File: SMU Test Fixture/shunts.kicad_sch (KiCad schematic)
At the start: 17 parts

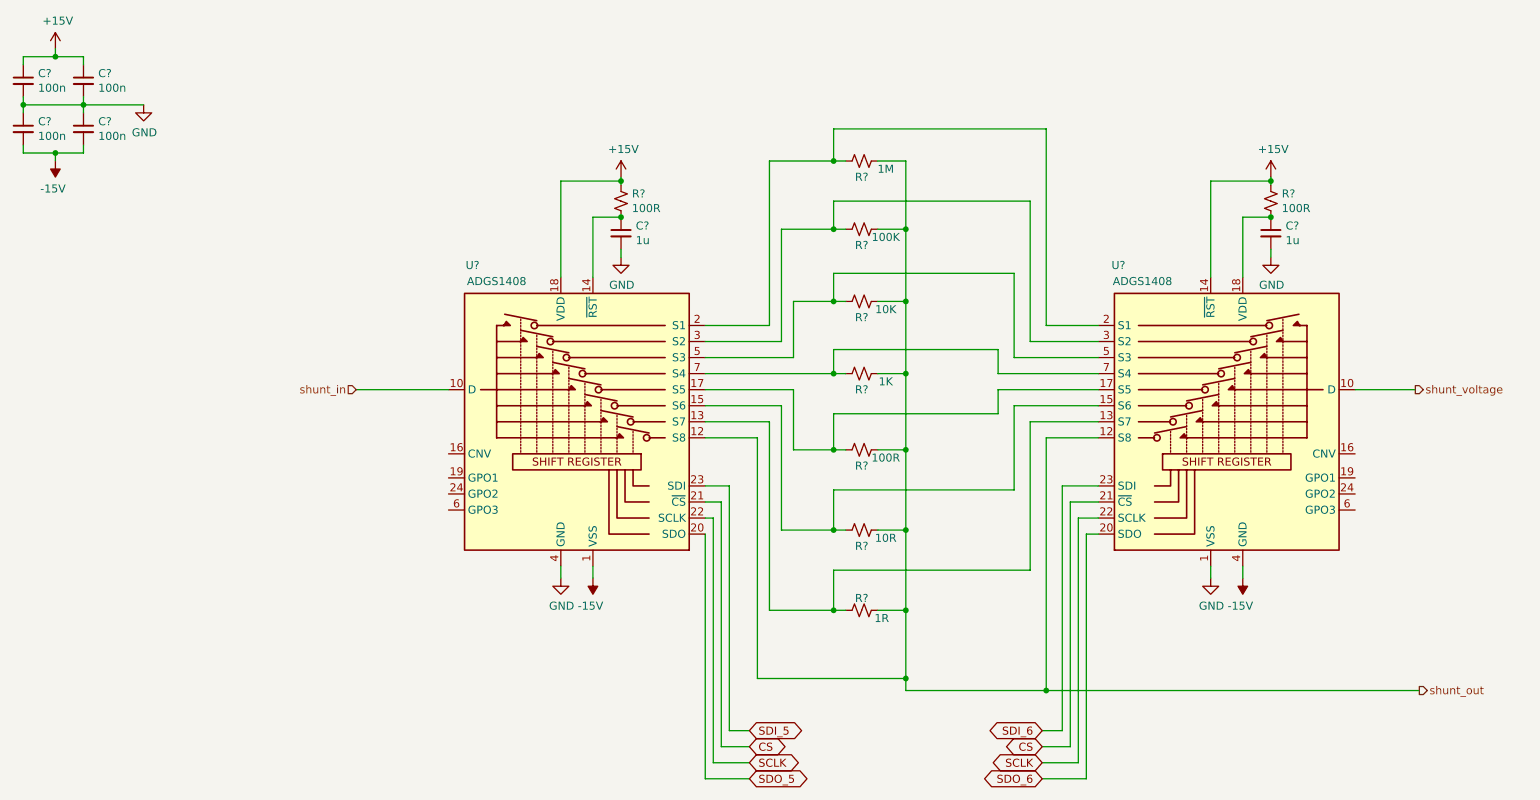
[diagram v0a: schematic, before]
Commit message: Fix grid nightmare. Begin adding bypass caps for a.switches
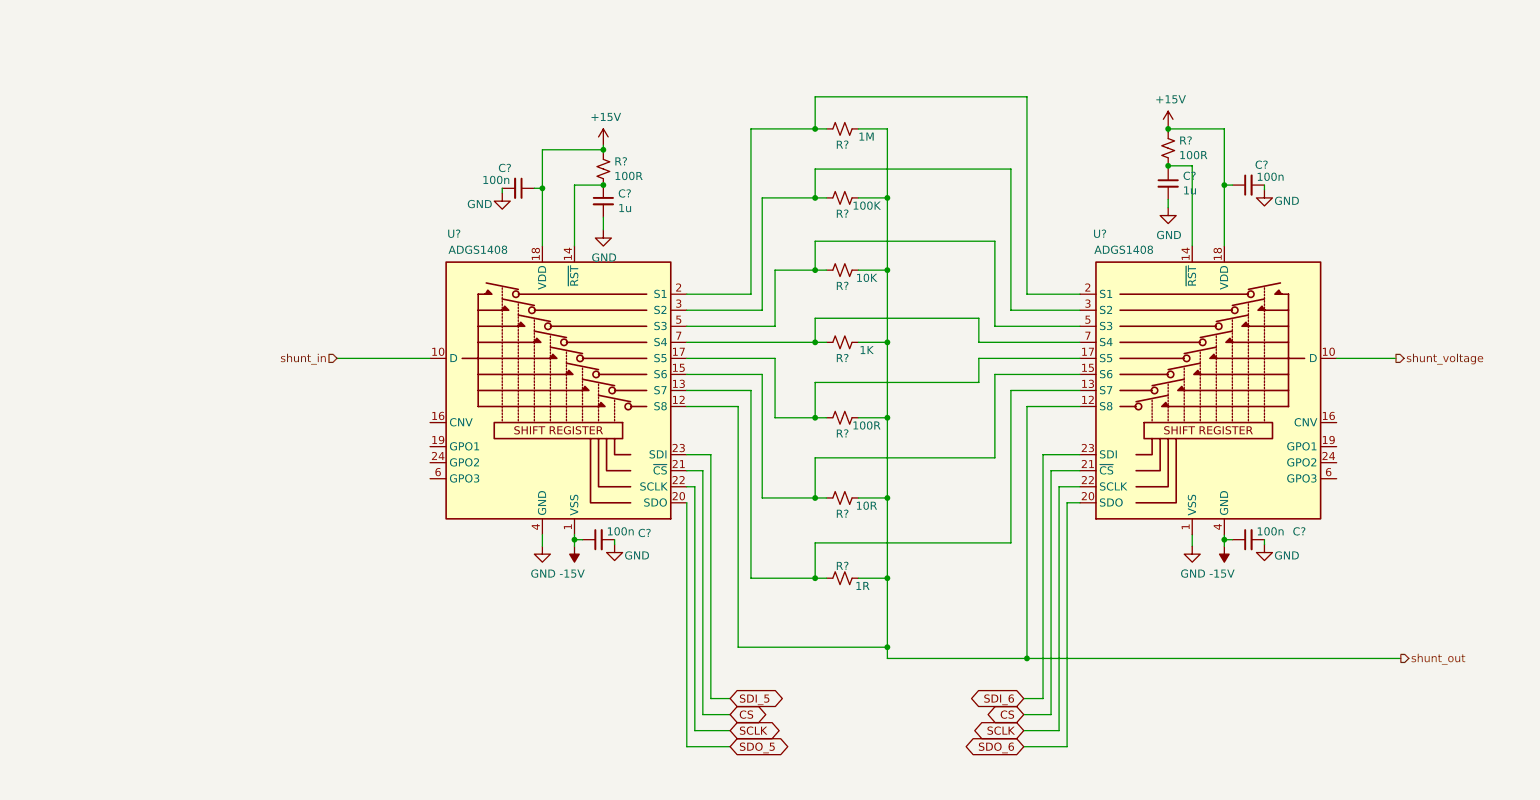
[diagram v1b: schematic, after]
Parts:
- removed C? (x4): 100n, Capacitor_SMD:C_0805_2012Metric_Pad1.18x1.45mm_HandSolder, symbol Device:C_Small
- added C? (x4): 100n, Capacitor_SMD:C_0805_2012Metric_Pad1.18x1.45mm_HandSolder, symbol Device:C_Small
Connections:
- net +15V: now also U?.18 (VDD), C?.1, C?.1; no longer U?.14 (~{RST})
- net -15V: now also C?.1, C?.1, C?.2, C?.2, C?.2, C?.2
- net at C?.1, R?.2: now also U?.14 (~{RST}); no longer U?.18 (VDD)
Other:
- moved on the sheet: C?, R?, U?

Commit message: Split ADGS1408 units, add switch contorl page
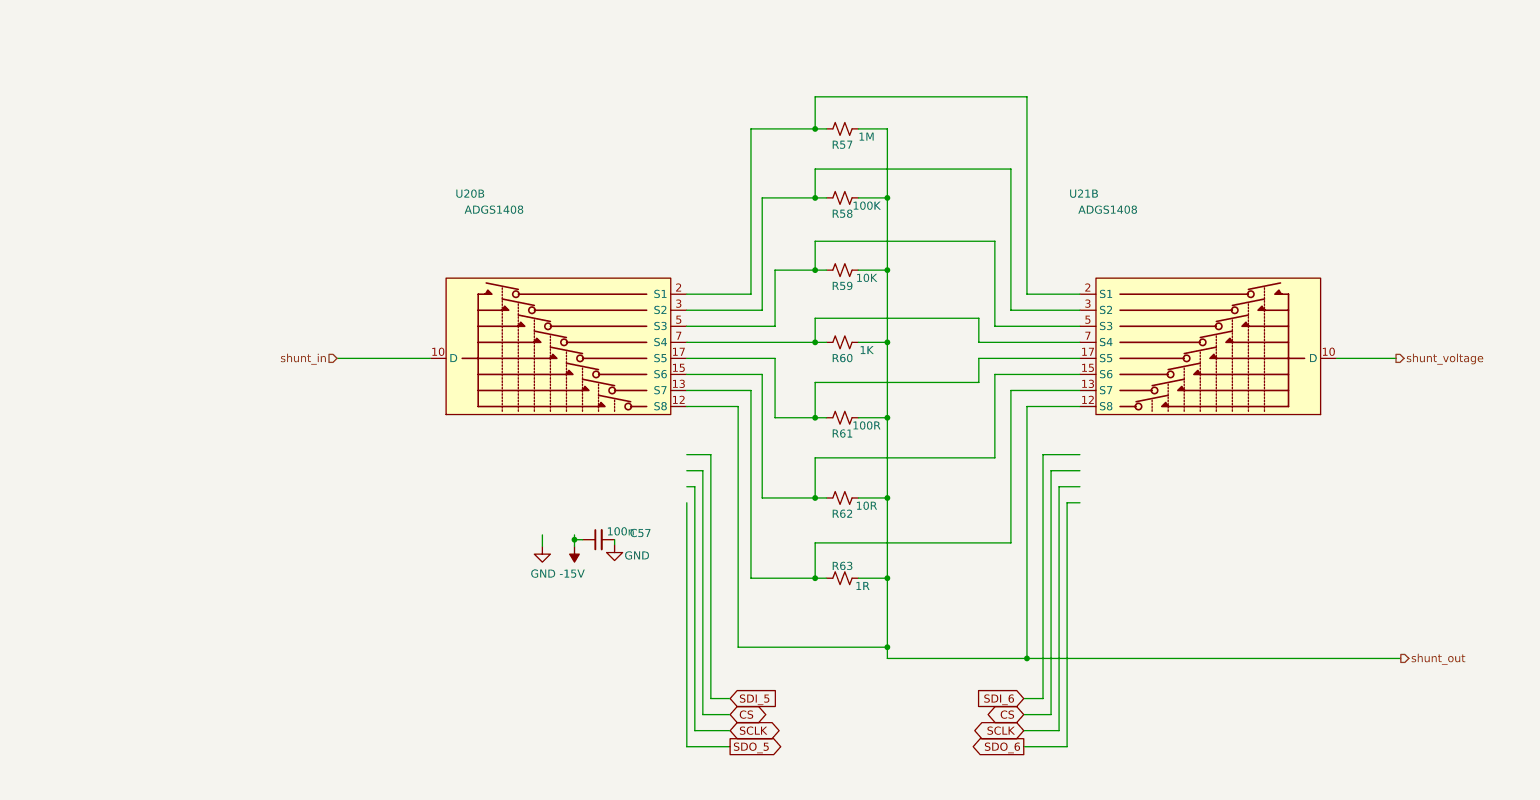
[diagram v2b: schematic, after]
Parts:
- removed C? (x2): 1u, symbol Device:C_Small
- removed C? (x3): 100n, Capacitor_SMD:C_0805_2012Metric_Pad1.18x1.45mm_HandSolder, symbol Device:C_Small
- removed R? (x2): 100R, symbol Device:R_Small_US
- gave numbers to parts that had none: 10
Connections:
- net -15V: no longer C57.2, U20.1 (VSS), U20.25 (VSS), U20.4 (GND), U21.1 (VSS), U21.25 (VSS), U21.4 (GND)
- net CS: no longer U20.21 (~{CS}), U21.21 (~{CS})
- net SCLK: no longer U20.22 (SCLK), U21.22 (SCLK)
- net SDI_5: no longer U20.23 (SDI)
- net SDI_6: no longer U21.23 (SDI)
- net SDO_5: no longer U20.20 (SDO)
- net SDO_6: no longer U21.20 (SDO)
- removed net +15V: U20.18 (VDD), U21.18 (VDD)
- new net GND: C57.2

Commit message: Symbol fixes, ERC pass
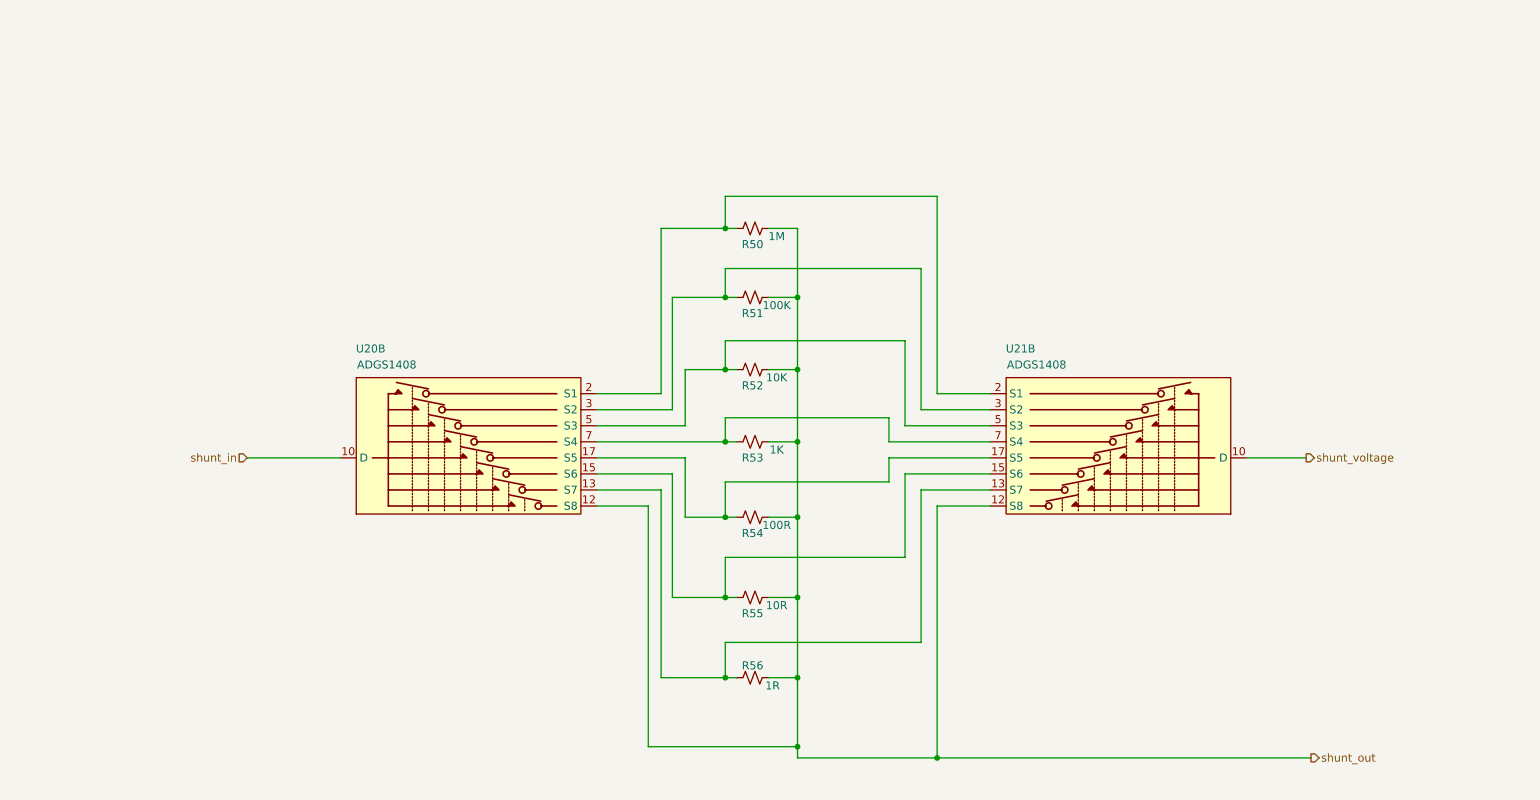
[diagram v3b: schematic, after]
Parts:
- removed C57: 100n, Capacitor_SMD:C_0805_2012Metric_Pad1.18x1.45mm_HandSolder, symbol Device:C_Small
- renumbered R57 to R50, R58 to R51, R59 to R52, R60 to R53, R61 to R54, R62 to R55, R63 to R56
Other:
- moved on the sheet: R50, R51, R52, R53, R54, R55, R56, U20B, U21B
